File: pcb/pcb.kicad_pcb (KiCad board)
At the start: 2 copper layers, 38 x 36 mm, 45 parts, among them J1 Conn_01x01_Socket, J2 Conn_01x02_Socket, J3 Conn_01x02_Socket, J4 Conn_01x01_Socket, K1 G3VM-31WR_TR05_, U1 AP2112K-3.3TRG1, U2 W25Q16JVUXIQ, U3 RP2040, U4 DS4432U+T&amp;R, U5 AD8403ARUZ1-REEL, Y2 Crystal_GND24_Small

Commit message: wip
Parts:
- removed J3: Conn_01x02_Socket, Connector_PinSocket_2.54mm:PinSocket_1x02_P2.54mm_Vertical
- removed J4: Conn_01x01_Socket, Connector_PinSocket_2.54mm:PinSocket_1x01_P2.54mm_Vertical
- J1: value Conn_01x01_Socket -> Conn_01x02_Socket; footprint Connector_PinSocket_2.54mm:PinSocket_1x01_P2.54mm_Vertical -> Connector_PinSocket_2.54mm:PinSocket_1x02_P2.54mm_Vertical
- J2: value Conn_01x02_Socket -> Conn_01x04_Socket; footprint Connector_PinSocket_2.54mm:PinSocket_1x02_P2.54mm_Vertical -> Connector_PinSocket_2.54mm:PinSocket_1x04_P2.54mm_Vertical
- moved J2 4.26 mm to (109.7, 52.1)
- moved J1 3.32 mm to (135.9, 52.1)
- moved R10 2.18 mm to (104.5, 63.4)
- moved K1 2.18 mm to (107.7, 64.8)
- moved R9 2.18 mm to (112.3, 67.6)
- moved U5 2.18 mm to (107.5, 71.1)
- moved C18 1.75 mm to (104.8, 75.9), turned to 180 degrees
- turned R7 to 180 degrees
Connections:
- J1 pad 1: Net-(J1-Pin_1) -> GND
- J2 pad 1: Net-(J2-Pin_1) -> UART_TX
- J2 pad 2: Net-(J2-Pin_2) -> UART_RX
- R3 pad 1: Net-(J1-Pin_1) -> Net-(J1-Pin_2)
- U3 pad 2: Net-(J3-Pin_1) -> UART_TX
- U3 pad 24: Net-(J2-Pin_1) -> Net-(J2-Pin_3)
- U3 pad 25: Net-(J2-Pin_2) -> Net-(J2-Pin_4)
- U3 pad 3: Net-(J3-Pin_2) -> UART_RX
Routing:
- net Net-(J2-Pin_4): track 0.00 -> 23.2 mm, vias 0 -> 1
- net Net-(J2-Pin_3): track 0.00 -> 20.5 mm, vias 0 -> 1
- net +3V3: track 47.4 -> 67.7 mm
- net POTS_SHDN: track 2.08 -> 21.8 mm, vias 0 -> 2
- net UART_RX: track 0.00 -> 19.2 mm, vias 0 -> 2
- net SPI_CS: track 1.91 -> 21.0 mm, vias 0 -> 2
- net SPI_TX: track 1.75 -> 19.7 mm, vias 0 -> 2
- net SPI_SCK: track 1.58 -> 19.2 mm, vias 0 -> 2
- net UART_TX: track 0.00 -> 17.3 mm, vias 0 -> 2
- net RELAY_A: track 7.96 -> 24.8 mm, vias 0 -> 2
- net 3DS_TP213_X-: track 0.00 -> 13.7 mm, vias 0 -> 2
- net Net-(J1-Pin_2): track 0.00 -> 12.2 mm, vias 0 -> 1
- net Net-(J1-Pin_1): track 12.2 -> 0.00 mm, vias 1 -> 0
- net 3DS_TP215_X+: track 0.00 -> 11.0 mm, vias 0 -> 2
- net 3DS_TP214_Y-: track 0.00 -> 5.13 mm
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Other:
- outline, holes or cut-outs redrawn

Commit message: pcb
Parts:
- moved J2 34.8 mm to (135.9, 75.0)
- turned R11 to 180 degrees
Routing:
- net 3DS_TP69_H: track 9.69 -> 44.8 mm, vias 0 -> 2
- net 3DS_TP68_V: track 10.2 -> 41.7 mm, vias 0 -> 2
- net 3DS_TP87_LEFT: track 0.89 -> 28.6 mm, vias 1 -> 2
- net 3DS_TP255_IRDA: track 1.55 -> 25.0 mm, vias 1 -> 2
- net 3DS_TP91_DOWN: track 1.06 -> 22.3 mm, vias 1 -> 2
- net 3DS_TP215_X+: track 11.0 -> 32.0 mm, vias 2 -> 4
- net 3DS_TP85_UP: track 1.13 -> 21.1 mm, vias 1 -> 2
- net 3DS_TP90_RIGHT: track 1.49 -> 20.6 mm, vias 1 -> 2
- net 3DS_TP213_X-: track 13.7 -> 31.9 mm, vias 2 -> 4
- net 3DS_TP58_WIFI: track 1.75 -> 19.4 mm, vias 1 -> 2
- net GND: track 5.80 -> 23.2 mm, vias 14 -> 30
- net 3DS_TP216_Y+: track 4.55 -> 20.2 mm
- net 3DS_TP52_POWER: track 2.82 -> 18.4 mm, vias 1 -> 2
- net 3DS_TP82_R: track 2.14 -> 17.2 mm, vias 1 -> 2
- net 3DS_TP81_SELECT: track 2.64 -> 17.6 mm, vias 1 -> 2
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- added copper zone on F.Cu, net 3DS_TP32_5V
- added copper zone on B.Cu, net GND
- added copper zone on F.Cu, net Net-(D1-K)
- added copper zone on F.Cu, net VBUS
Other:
- board size 38 x 36 mm -> 35.5 x 27 mm

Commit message: pcb
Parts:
- removed K1: G3VM-31WR_TR05_, G3VM-31WR_TR05_:G3VM-31WR_TR05_
- removed R10: 430, Resistor_SMD:R_0402_1005Metric
- added C19: 100n, Capacitor_SMD:C_0402_1005Metric, F.Cu at (108.0, 60.1)
- added U6: ADG801BRTZ-REEL7, ADG801BRTZ-REEL7:SOT-23-6_L2.9-W1.6-P0.95-LS2.8-BL, F.Cu at (108.5, 63.0)
- Y2: footprint Crystal:Crystal_SMD_2520-4Pin_2.5x2.0mm -> Crystal:Crystal_SMD_3225-4Pin_3.2x2.5mm
- moved R11 4.99 mm to (124.7, 75.5)
- moved D3 4.99 mm to (124.7, 74.6)
- moved U5 2.27 mm to (109.7, 71.6)
- moved R9 1.60 mm to (112.8, 66.1)
- moved C4 1.43 mm to (111.9, 57.4)
- moved C18 1.29 mm to (105.1, 74.7), turned to 90 degrees
- moved D1 0.74 mm to (131.8, 69.6)
- moved D2 0.74 mm to (131.8, 71.0)
- moved Y2 0.41 mm to (112.6, 59.9)
- moved C12 0.21 mm to (119.1, 68.8)
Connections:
- FPC1 pad 25: GND -> unconnected-(FPC1-Pad25)
- FPC1 pad 26: GND -> unconnected-(FPC1-Pad26)
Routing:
- net +3V3: track 67.7 -> 88.6 mm, vias 0 -> 2
- net 3DS_TP215_X+: track 32.0 -> 41.9 mm, vias 4 -> 2
- net RELAY_A: track 22.9 -> 13.3 mm
- net 3DS_TP69_H: track 44.8 -> 36.0 mm
- net 3DS_TP214_Y-: track 19.5 -> 28.2 mm, vias 0 -> 2
- net 3DS_TP216_Y+: track 20.2 -> 28.3 mm, vias 0 -> 2
- net 3DS_TP68_V: track 41.7 -> 33.6 mm
- net Net-(J2-Pin_3): track 27.1 -> 20.9 mm
- net Net-(D1-K): track 7.32 -> 1.30 mm
- net Net-(D3-A): track 4.05 -> 9.85 mm
- net 3DS_TP87_LEFT: track 28.6 -> 24.0 mm
- net 3DS_TP213_X-: track 31.9 -> 36.2 mm, vias 4 -> 2
- net Net-(J2-Pin_4): track 23.2 -> 19.4 mm
- net Net-(U5-W2): track 2.87 -> 6.58 mm
- net GND: track 23.2 -> 20.0 mm, vias 30 -> 46
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- added copper zone on F.Cu, net D+
- added copper zone on F.Cu, net D-
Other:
- board size 35.5 x 27 mm -> 34.3 x 27 mm
- board text added: "100n"

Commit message: flex
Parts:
- added TP1: TestPoint, TestPoint:TestPoint_Pad_D1.5mm, F.Cu at (135.9, 70.5)
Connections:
- net Net-(U3-USB_DM) renamed /USB_D-
- net Net-(U3-USB_DP) renamed /USB_D+

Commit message: Order ready
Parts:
- C4, C5: value 15p -> 10p
- R11: value 91 -> 24
- moved C18 2.92 mm to (107.6, 76.2), turned to 180 degrees
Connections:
- U3 pad 26: unconnected-(U3-RUN-Pad26) -> +3V3
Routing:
- net GND: track 20.0 -> 26.1 mm, vias 46 -> 43
- net UART_RX: track 27.2 -> 21.5 mm
- net UART_TX: track 26.8 -> 21.1 mm
- net +3V3: track 88.6 -> 93.3 mm, vias 2 -> 4
- net RELAY_A: track 13.3 -> 15.2 mm
- net Net-(J1-Pin_2): track 12.2 -> 14.0 mm
- net Net-(J2-Pin_3): track 20.9 -> 21.9 mm
- net Net-(J2-Pin_4): track 19.4 -> 20.4 mm
- net 3DS_TP255_IRDA: track 25.2 -> 26.2 mm
- net 3DS_TP87_LEFT: track 24.0 -> 24.8 mm
- added copper zone on B.Cu, net +1V1
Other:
- board size 34.3 x 27 mm -> 33.6 x 27 mm

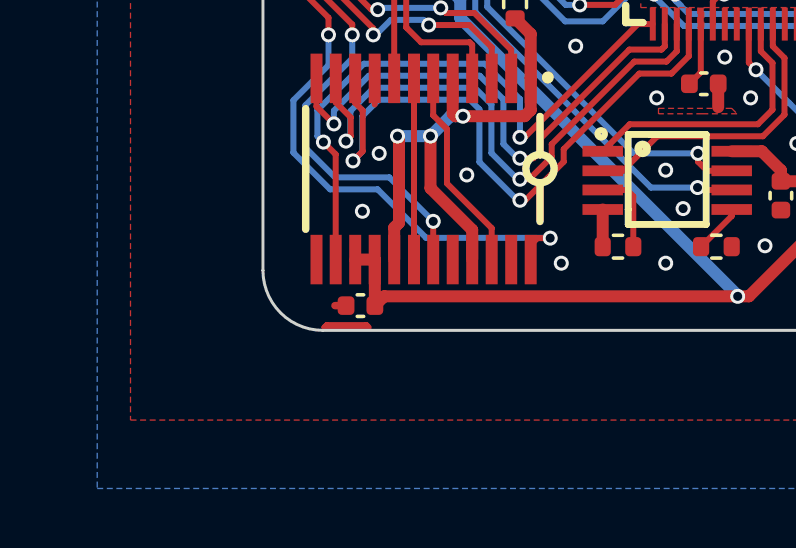
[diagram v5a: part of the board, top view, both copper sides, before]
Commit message: Slight adjustment of GND wiring
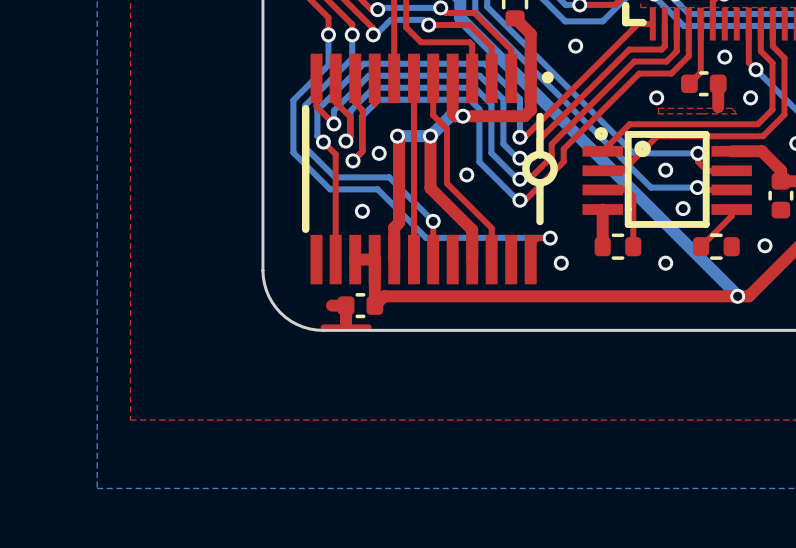
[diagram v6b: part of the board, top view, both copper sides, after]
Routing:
- net GND: track 26.1 -> 25.3 mm

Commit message: Add silkscreen of logo on PCB
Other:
- board text added: "NeoControllerMod"
- board text added: "v1.0"

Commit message: Change name
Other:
- board text added: "NeoCtrlMod"
- board text removed: "NeoControllerMod"
